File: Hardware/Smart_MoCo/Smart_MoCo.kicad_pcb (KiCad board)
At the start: 2 copper layers, 52.8 x 53.3 mm, 57 parts, among them J1 Conn_02x02_Counter_Clockwise, Q1 BSS138, Q2 BSS138, Q3 BSS138, U1 VNH5019A-E, U2 STM32F042F6Px, U3 ATA6561, U4 AP62200WU, U5 AP62200WU

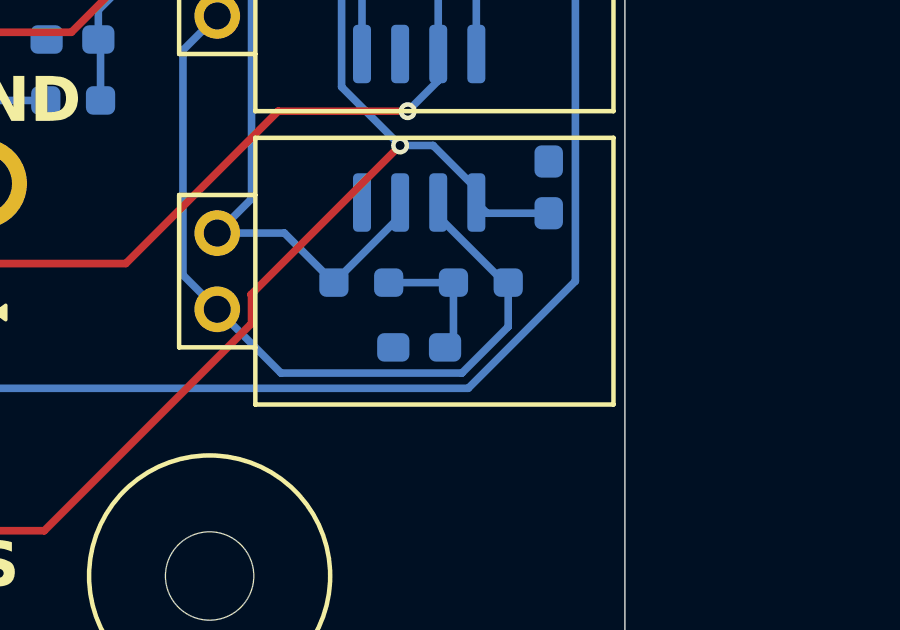
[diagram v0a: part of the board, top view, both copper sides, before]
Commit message: Modify CAN circuit
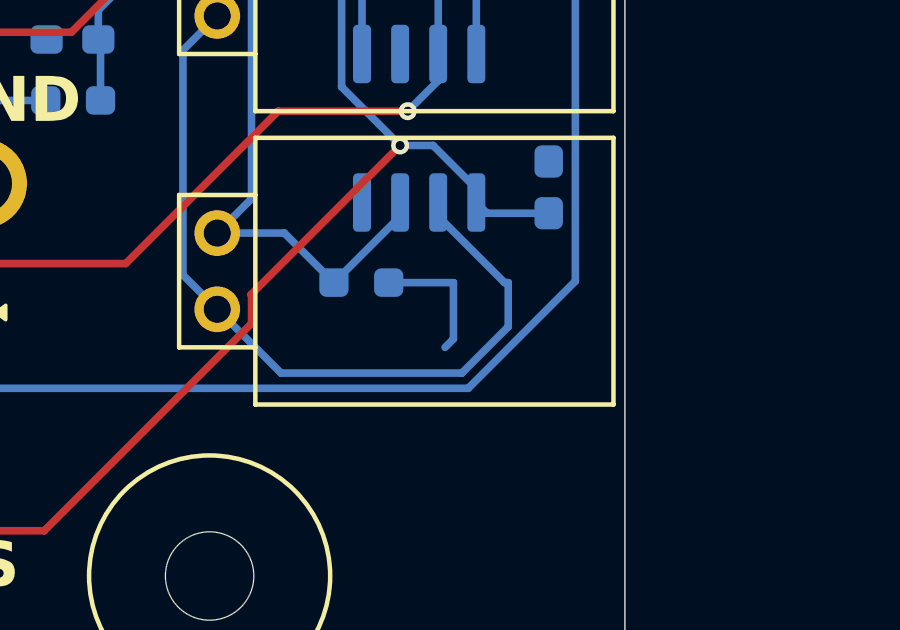
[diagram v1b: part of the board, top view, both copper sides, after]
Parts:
- removed C10: 4.7nF, Capacitor_SMD:C_0603_1608Metric_Pad1.08x0.95mm_HandSolder
- removed R6: 60, Resistor_SMD:R_0603_1608Metric_Pad0.98x0.95mm_HandSolder
- R5: value 60 -> 120
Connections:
- R5 pad 2: Net-(C10-Pad1) -> CANL
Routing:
- net CANL: track 27.1 -> 31.6 mm
- net Net-(C10-Pad1): track 4.43 -> 0.00 mm

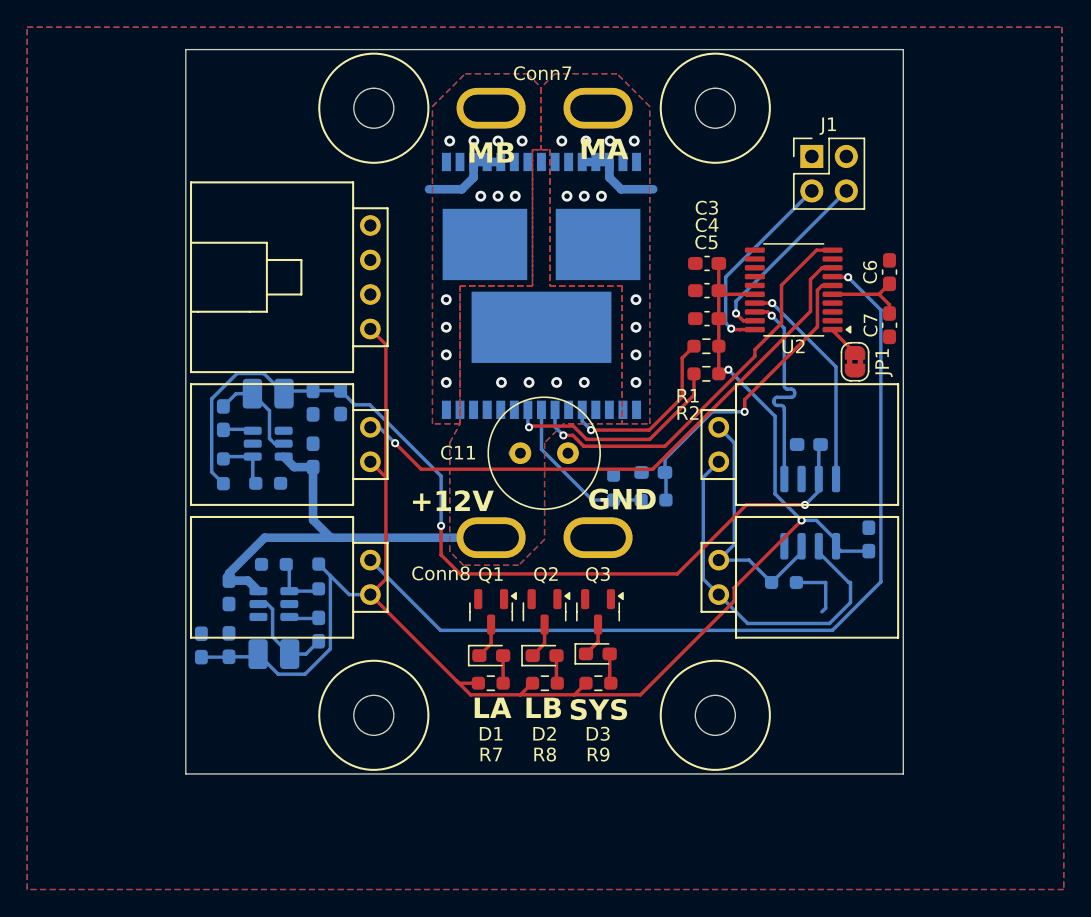
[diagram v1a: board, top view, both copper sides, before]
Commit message: Implement schematic first review feedback and finish PCB layout
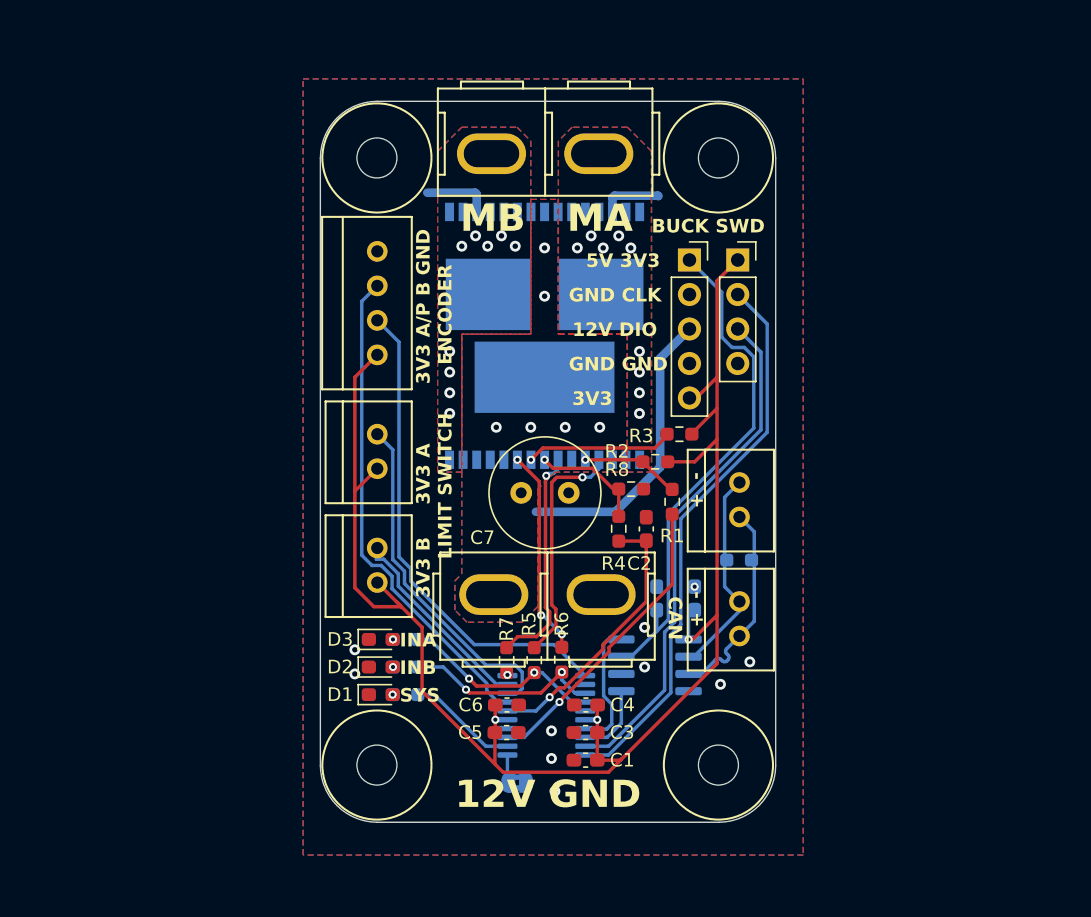
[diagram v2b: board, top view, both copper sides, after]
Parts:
- removed C11: 330uF, Capacitor_THT:C_Radial_D8.0mm_H11.5mm_P3.50mm
- removed C12, C16: 10uF, Capacitor_SMD:C_0603_1608Metric_Pad1.08x0.95mm_HandSolder
- removed C13, C17: 100nF, Capacitor_SMD:C_0603_1608Metric_Pad1.08x0.95mm_HandSolder
- removed C14, C15, C18, C19: 22uF, Capacitor_SMD:C_0603_1608Metric_Pad1.08x0.95mm_HandSolder
- removed Conn8: AndersonPP, MRDT_Connectors:Square_Anderson_2_H_Side_By_Side
- removed L1: 4.7uH, Inductor_SMD:L_1008_2520Metric_Pad1.43x2.20mm_HandSolder
- removed L2: 3.3uH, Inductor_SMD:L_1008_2520Metric_Pad1.43x2.20mm_HandSolder
- removed Q1, Q2, Q3: BSS138, Package_TO_SOT_SMD:SOT-23
- removed R13: 33.2, Resistor_SMD:R_0603_1608Metric_Pad0.98x0.95mm_HandSolder
- removed U4, U5: AP62200WU, Package_TO_SOT_SMD:TSOT-23-6
- added C2: 33nF, Capacitor_SMD:C_0603_1608Metric_Pad1.08x0.95mm_HandSolder, F.Cu at (159.9, 87.7)
- added Conn1: Molex_SL_02, MRDT_Connectors:MOLEX_SL_02_Vertical, F.Cu at (166.8, 86.9)
- added J2: Conn_01x05, Connector_PinSocket_2.54mm:PinSocket_1x05_P2.54mm_Vertical, F.Cu at (163.1, 67.9)
- added R6: 1k, Resistor_SMD:R_0603_1608Metric_Pad0.98x0.95mm_HandSolder, F.Cu at (153.7, 97.4)
- C1: value 33nF -> 100nF; moved to F.Cu
- C4: value 100nF -> 4.7uF
- C5: value 4.7uF -> 10nF
- C6: value 10nF -> 1uF
- C7: value 1uF -> 330uF; footprint Capacitor_SMD:C_0603_1608Metric_Pad1.08x0.95mm_HandSolder -> Capacitor_THT:C_Radial_D8.0mm_H11.5mm_P3.50mm
- Conn2, Conn5: footprint Library:MOLEX_SL_02_Horizontal_No_Holes -> MRDT_Connectors:MOLEX_SL_02_Vertical
- Conn3: value Molex_SL_02 -> Molex_SL_04; footprint Library:MOLEX_SL_02_Horizontal_No_Holes -> MRDT_Connectors:MOLEX_SL_04_Vertical
- Conn4: value Molex_SL_04 -> Molex_SL_02; footprint Library:MOLEX_SL_04_Horizontal_No_Holes -> MRDT_Connectors:MOLEX_SL_02_Vertical
- Conn6: value Molex_SL_02 -> AndersonPP; footprint Library:MOLEX_SL_02_Horizontal_No_Holes -> MRDT_Connectors:Square_Anderson_2_V_Side_By_Side
- Conn7: footprint MRDT_Connectors:Square_Anderson_2_H_Side_By_Side -> MRDT_Connectors:Square_Anderson_2_V_Side_By_Side
- D1: value Blue -> Red
- D3: value Red -> Blue
- J1: value Conn_02x02_Counter_Clockwise -> Conn_01x04; footprint Connector_PinHeader_2.54mm:PinHeader_2x02_P2.54mm_Vertical -> Connector_PinSocket_2.54mm:PinSocket_1x04_P2.54mm_Vertical
- JP1: moved to B.Cu
- R1: value 3.3k -> 1k
- R10: value 52.3k -> 220
- R11: value 56.2k -> 220
- R12: value 31.6k -> 220
- R3: value 10k -> 3.3k; moved to F.Cu
- R4: value 1.5k -> 10k; moved to F.Cu
- R5: value 120 -> 1k; moved to F.Cu
- R7: value 220 -> 1k
- R8: value 220 -> 1.5k
- R9: value 220 -> 120; moved to B.Cu
- U1: value VNH5019A-E -> STM32F042F6Px; footprint Package_SO:ST_MultiPowerSO-30 -> Package_SO:TSSOP-20_4.4x6.5mm_P0.65mm
- U2: value STM32F042F6Px -> VNH5019A-E; footprint Package_SO:TSSOP-20_4.4x6.5mm_P0.65mm -> Package_SO:ST_MultiPowerSO-30; moved to B.Cu
- moved C6 42.5 mm to (149.6, 100.7), turned to 0 degrees
- moved JP1 39.7 mm to (150.4, 106.4), turned to 180 degrees
- moved C3 35.7 mm to (155.4, 102.7)
- moved Conn7 35.6 mm to (152.7, 92.5), turned to 0 degrees
- moved C5 33.9 mm to (149.6, 102.7), turned to 0 degrees
- moved C4 31.8 mm to (155.4, 100.7)
- moved U1 31.6 mm to (152.5, 101.5), turned to 0 degrees
- moved C7 29.8 mm to (150.7, 85.1), turned to 0 degrees
- moved Conn3 29.3 mm to (140.1, 74.9), turned to 90 degrees
- moved Conn6 25.9 mm to (152.4, 60.2), turned to 180 degrees
- moved C1 21.8 mm to (155.4, 104.8), turned to 180 degrees
- moved R10 21.2 mm to (142.2, 99.9), turned to 180 degrees
- moved R5 19.3 mm to (151.6, 97.4), turned to -90 degrees
- moved U2 18.7 mm to (152.4, 73.5), turned to 90 degrees
- moved R11 16.9 mm to (142.2, 97.9), turned to 180 degrees
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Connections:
- C1 pad 1: GND -> +3V3
- C1 pad 2: CS -> GND
- C7 pad 1: +3V3 -> +12V
- Conn3 pad 1: CANH -> +3V3
- Conn3 pad 2: CANL -> ENC_A/PWM
- Conn4 pad 2: ENC_A -> LIM_A
- Conn5 pad 2: LIM_A -> LIM_B
- Conn6 pad 1: +3V3 -> /OUTA
- Conn6 pad 2: LIM_B -> /OUTB
- Conn7 pad 1: /OUTA -> +12V
- Conn7 pad 2: /OUTB -> GND
- D1 pad 1: Net-(D1-K) -> GND
- D2 pad 1: Net-(D2-K) -> GND
- D3 pad 1: Net-(D3-K) -> GND
- J1 pad 2: GND -> SWCLK
- J1 pad 3: SWCLK -> SWDIO
- J1 pad 4: SWDIO -> GND
- R1 pad 1: +3V3 -> Net-(U2-EN/DIAGA)
- R1 pad 2: DIAGA -> DIAG_A
- R10 pad 1: +5V -> LED_STATUS
- R10 pad 2: Net-(U4-FB) -> Net-(D1-A)
- R11 pad 1: Net-(U4-FB) -> IN_B
- R11 pad 2: GND -> Net-(D2-A)
- R12 pad 1: +3V3 -> IN_A
- R12 pad 2: Net-(U5-FB) -> Net-(D3-A)
- R2 pad 2: Net-(U1-EN/DIAGB) -> Net-(U2-EN/DIAGA)
- R3 pad 1: Net-(U1-CS) -> +3V3
- R3 pad 2: CS -> Net-(U2-EN/DIAGB)
- R4 pad 1: Net-(U1-CS) -> Net-(U2-CS)
- R4 pad 2: GND -> CS
- R5 pad 1: CANH -> Net-(U2-INA)
- R5 pad 2: CANL -> IN_A
- R7 pad 1: +3V3 -> Net-(U2-PWM)
- R7 pad 2: Net-(D1-A) -> PWM
- R8 pad 1: +3V3 -> Net-(U2-CS)
- R8 pad 2: Net-(D2-A) -> GND
- R9 pad 1: +3V3 -> CANH
- R9 pad 2: Net-(D3-A) -> CANL
- U1 pad 1: /OUTA -> Net-(JP1-B)
- U1 pad 10: INB -> PWM
- U1 pad 11: unconnected-(U1-CP-Pad11) -> ENC_A/PWM
- U1 pad 12: +12V -> unconnected-(U1-PA6-Pad12)
- U1 pad 13: +12V -> IN_B
- U1 pad 14: unconnected-(U1-NC-Pad14) -> IN_A
- U1 pad 15: /OUTB -> GND
- U1 pad 16: /OUTB -> +3V3
- U1 pad 17: unconnected-(U1-NC-Pad17) -> CAN_RX
- U1 pad 18: GND -> CAN_TX
- U1 pad 19: GND -> SWDIO
- U1 pad 2: unconnected-(U1-NC-Pad2) -> LED_STATUS
- U1 pad 20: GND -> SWCLK
- U1 pad 3: +12V -> DIAG_A
- U1 pad 4: INA -> unconnected-(U1-NRST-Pad4)
- U1 pad 5: DIAGA -> +3V3
- U1 pad 6: GND -> CS
- U1 pad 7: PWM -> ENC_B
- U1 pad 8: Net-(U1-CS) -> LIM_A
- U1 pad 9: Net-(U1-EN/DIAGB) -> LIM_B
- U2 pad 1: Net-(JP1-B) -> /OUTA
- U2 pad 10: PWM -> Net-(U2-INB)
- U2 pad 11: ENC_A -> unconnected-(U2-CP-Pad11)
- U2 pad 12: ENC_A -> +12V
- U2 pad 13: ENC_B -> +12V
- U2 pad 14: LED_LIM_A -> unconnected-(U2-NC-Pad14)
- U2 pad 15: GND -> /OUTB
- U2 pad 16: +3V3 -> /OUTB
- U2 pad 17: CAN_RX -> unconnected-(U2-NC-Pad17)
- U2 pad 18: CAN_TX -> GND
- U2 pad 19: SWDIO -> GND
- U2 pad 2: LED_STATUS -> unconnected-(U2-NC-Pad2)
- U2 pad 20: SWCLK -> GND
- U2 pad 3: unconnected-(U2-PF1-Pad3) -> +12V
- U2 pad 4: unconnected-(U2-NRST-Pad4) -> Net-(U2-INA)
- U2 pad 5: +3V3 -> Net-(U2-EN/DIAGA)
- U2 pad 6: CS -> GND
- U2 pad 7: LIM_A -> Net-(U2-PWM)
- U2 pad 8: LIM_B -> Net-(U2-CS)
- U2 pad 9: LED_LIM_B -> Net-(U2-EN/DIAGB)
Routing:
- net LIM_A: track 65.8 -> 25.6 mm, vias 1 -> 0
- net ENC_B: track 0.00 -> 36.4 mm
- net ENC_A/PWM: track 0.00 -> 35.9 mm
- net +5V: track 67.8 -> 37.1 mm, vias 2 -> 0
- net PWM: track 30.2 -> 0.00 mm
- net LIM_B: track 42.8 -> 14.8 mm, vias 1 -> 0
- net SWCLK: track 14.7 -> 41.4 mm, vias 1 -> 0
- net SWDIO: track 14.0 -> 37.8 mm, vias 1 -> 0
- net DIAG_A: track 0.00 -> 22.2 mm, vias 0 -> 1
- net Net-(U2-INA): track 0.00 -> 17.5 mm, vias 0 -> 1
- net Net-(U1-EN/DIAGB): track 16.8 -> 0.00 mm, vias 1 -> 0
- net Net-(U2-PWM): track 0.00 -> 16.7 mm, vias 0 -> 1
- net CANL: track 31.6 -> 15.1 mm
- net Net-(U2-INB): track 0.00 -> 15.2 mm, vias 0 -> 3
- net IN_A: track 0.00 -> 15.1 mm, vias 0 -> 2
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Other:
- board size 52.8 x 53.3 mm -> 33.5 x 53.1 mm
- board text added: "- +"
- board text added: "12V DIO"
- board text added: "12V GND"
- board text added: "3V3"
- board text added: "3V3 A/P B GND ENCODER"
- board text added: "3V3 B 3V3 A LIMIT SWITCH"
- board text added: "5V 3V3"
- board text added: "BUCK SWD"
- board text added: "CAN"
- board text added: "GND CLK"
- board text added: "GND GND"
- board text added: "INA"
- board text added: "INB"
- board text removed: "+12V"
- board text removed: "GND"
- board text removed: "LA"
- board text removed: "LB"

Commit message: Prepare for board review
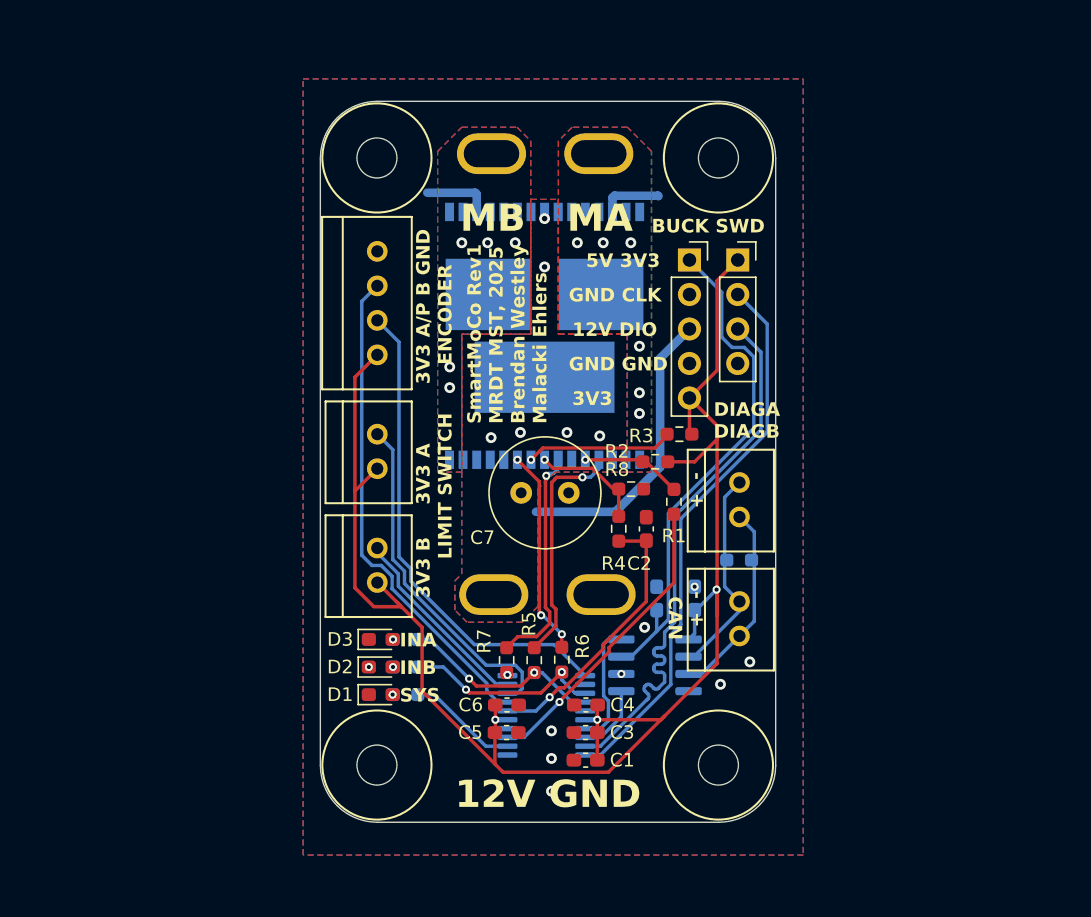
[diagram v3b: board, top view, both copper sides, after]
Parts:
- removed JP1: SolderJumper_2_Bridged, Jumper:SolderJumper-2_P1.3mm_Bridged2Bar_RoundedPad1.0x1.5mm
- added G***: LOGO, MRDT_Silkscreens:0_MRDT_Logo_7.5mm, B.Cu at (145.0, 86.6)
- added G***: LOGO, Local Libraries:signature_Malacki_Ehlers, B.Cu at (153.5, 89.3)
- added REF**: signature_Brendan_Westley, Local Libraries:signature_Brendan_Westley, B.Cu at (160.3, 87.5)
- Conn6, Conn7: footprint MRDT_Connectors:Square_Anderson_2_V_Side_By_Side -> Local Libraries:Square_Anderson_2_V_Side_By_Side_No_Silkscreen
- D2, D3: value Blue -> Orange
- moved R1 0.13 mm to (161.9, 85.7)
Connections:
- U1 pad 1: Net-(JP1-B) -> GND
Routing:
- net +3V3: track 118.0 -> 121.9 mm
- net SWDIO: track 37.8 -> 40.9 mm
- net Net-(JP1-B): track 1.96 -> 0.00 mm
- net CANH: track 15.4 -> 14.6 mm
- net LIM_B: track 14.8 -> 14.1 mm
- net GND: vias 10 -> 9
- net /OUTB: vias 9 -> 5
- net /OUTA: vias 9 -> 6
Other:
- board text added: "DIAGA DIAGB"
- board text added: "SmartMoCo Rev1 MRDT MST, 2025 Brendan Westley Malacki Ehlers"

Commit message: Update LED resistor values
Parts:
- removed the G*** at (145.0, 86.6)
- removed REF**: signature_Brendan_Westley, Local Libraries:signature_Brendan_Westley
- R10, R11, R12: value 220 -> 1k

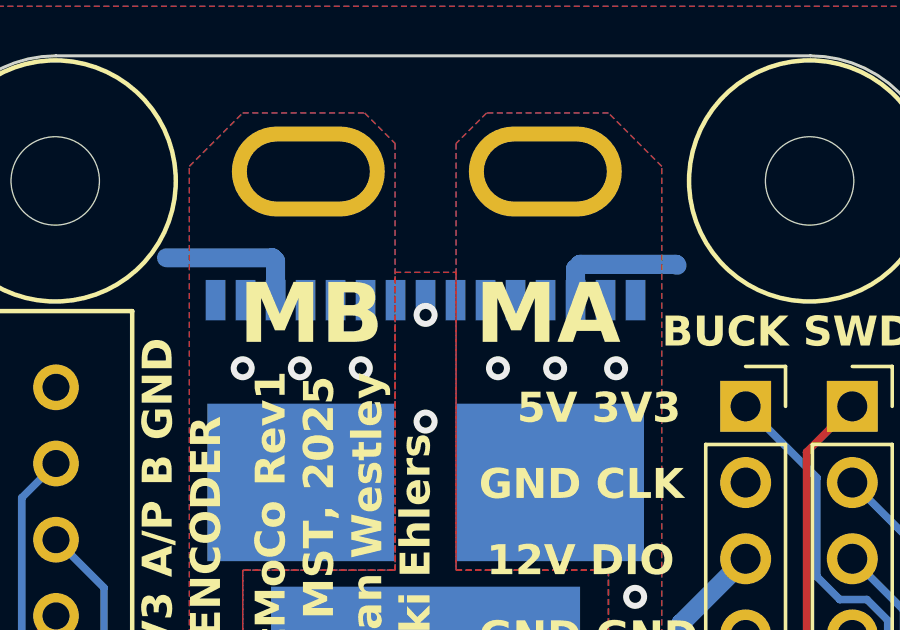
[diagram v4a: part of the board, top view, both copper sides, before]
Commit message: Implement board review changes
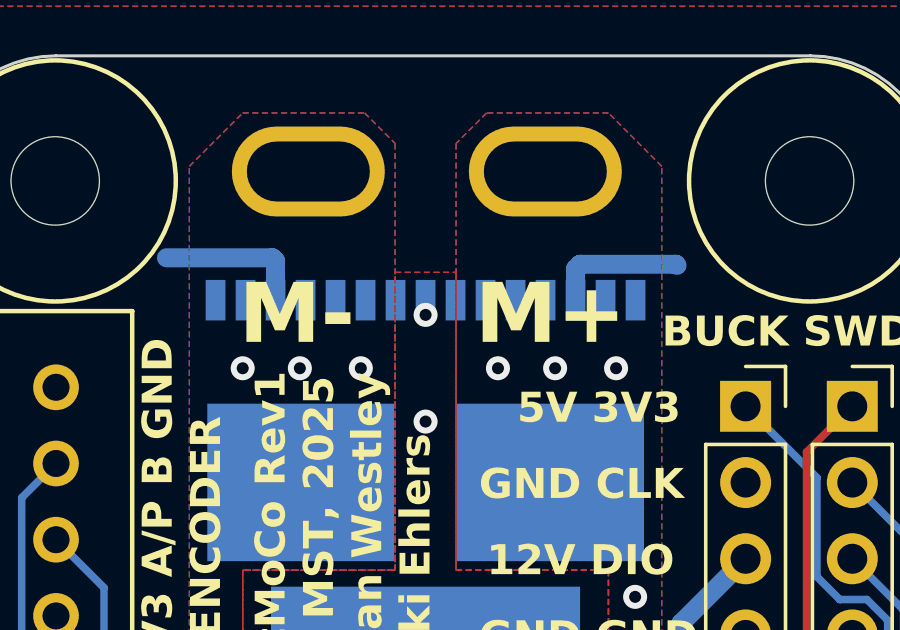
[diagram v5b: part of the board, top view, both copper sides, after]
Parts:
- added G***: LOGO, MRDT_Silkscreens:0_MRDT_Logo_7.5mm, B.Cu at (145.0, 86.9)
- added REF**: signature_Brendan_Westley, Local Libraries:signature_Brendan_Westley, B.Cu at (160.4, 87.5)
- moved G*** 0.90 mm to (154.2, 89.9)
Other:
- board text added: "M+"
- board text added: "M-"
- board text removed: "MA"
- board text removed: "MB"
